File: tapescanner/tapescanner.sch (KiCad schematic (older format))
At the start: 49 parts, among them J0 USB_B, J2 AVR-ISP-10, M0 Motor_DC, Q0 TEPT5600, Q1 TEPT5600, Q10 MJE13007G, Q2 TEPT5600, Q3 TEPT5600, Q4 TEPT5600, Q5 TEPT5600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

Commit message: Fix RKM codes
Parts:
- C2: value 10nF -> 10n
- C3, C4: value 47pF -> 47p
- C5: value 4.7uF -> 4.7u
- C6: value 100nF -> 100n
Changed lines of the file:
@@
 P 3750 2500
 F 0 "C2" H 3865 2546 50  0000 L CNN
-F 1 "10nF" H 3865 2455 50  0000 L CNN
+F 1 "10n" H 3865 2455 50  0000 L CNN
 F 2 "" H 3788 2350 50  0001 C CNN
 F 3 "~" H 3750 2500 50  0001 C CNN
@@
 P 4200 2500
 F 0 "C3" H 4315 2546 50  0000 L CNN
-F 1 "47pF" H 4315 2455 50  0000 L CNN
+F 1 "47p" H 4315 2455 50  0000 L CNN
 F 2 "" H 4238 2350 50  0001 C CNN
 F 3 "~" H 4200 2500 50  0001 C CNN
@@
 P 4650 2500
 F 0 "C4" H 4765 2546 50  0000 L CNN
-F 1 "47pF" H 4765 2455 50  0000 L CNN
+F 1 "47p" H 4765 2455 50  0000 L CNN
 F 2 "" H 4688 2350 50  0001 C CNN
 F 3 "~" H 4650 2500 50  0001 C CNN
@@
 P 4900 1350
 F 0 "C6" H 5015 1396 50  0000 L CNN
-F 1 "100nF" H 5015 1305 50  0000 L CNN
+F 1 "100n" H 5015 1305 50  0000 L CNN
 F 2 "" H 4938 1200 50  0001 C CNN
 F 3 "~" H 4900 1350 50  0001 C CNN
@@
 U 1 1 6084B0AF
 P 4400 1350
-F 0 "C5" H 4518 1396 50  0000 L CNN
-F 1 "4.7uF" H 4518 1305 50  0000 L CNN
+F 0 "C5" H 4282 1304 50  0000 R CNN
+F 1 "4.7u" H 4282 1395 50  0000 R CNN
 F 2 "" H 4438 1200 50  0001 C CNN
 F 3 "~" H 4400 1350 50  0001 C CNN

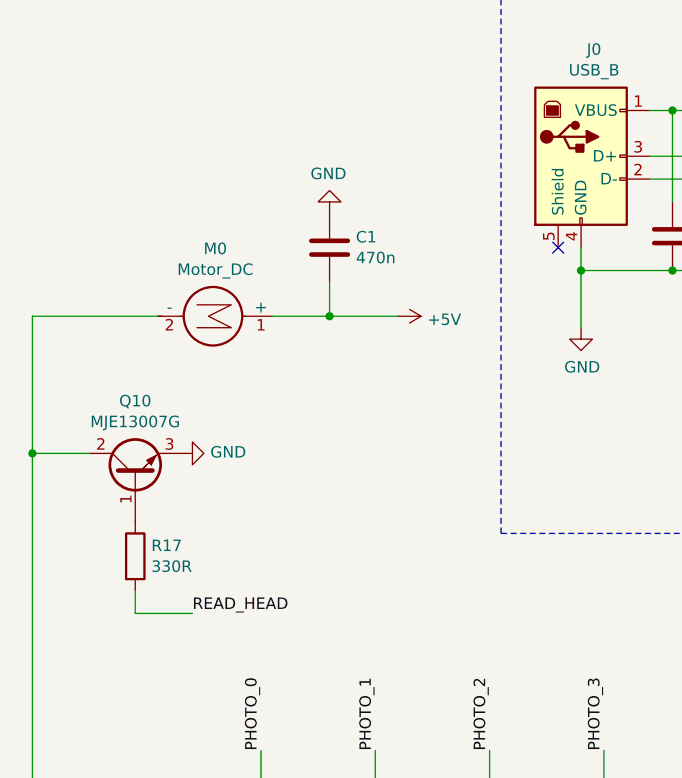
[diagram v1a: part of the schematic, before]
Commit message: Fix motor capacitor
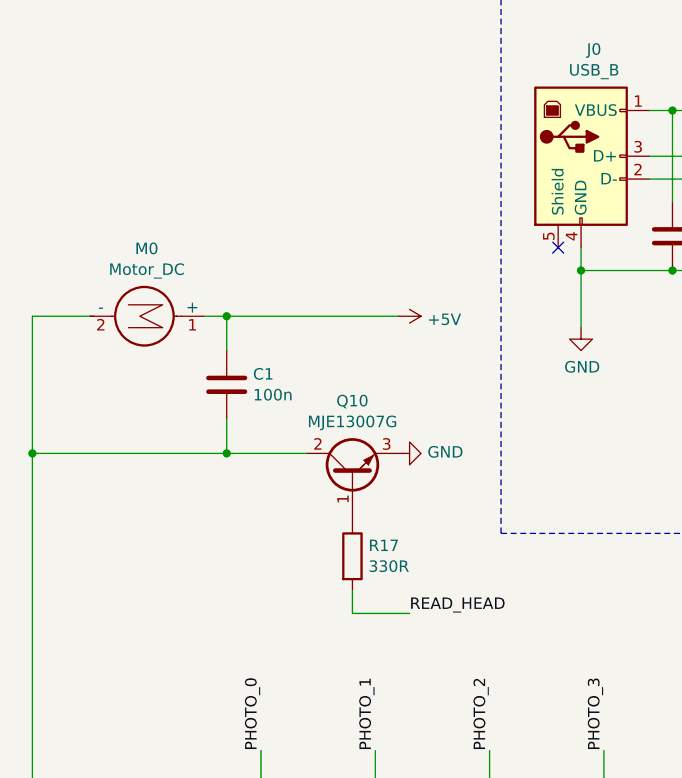
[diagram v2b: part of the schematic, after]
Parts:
- C1: value 470n -> 100n
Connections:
- net +5V: now also C1.1; no longer C1.2
- net GND: no longer C1.1
- net at D0.1 (K), D1.1 (K), D2.1 (K)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: now also C1.2
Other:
- moved on the sheet: M0, Q10, R17
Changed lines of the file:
@@
 L Transistor_BJT:MJE13007G Q10
 U 1 1 606AAE77
-P 1400 3550
-F 0 "Q10" V 1729 3550 50  0000 C CNN
-F 1 "MJE13007G" V 1638 3550 50  0000 C CNN
-F 2 "Package_TO_SOT_THT:TO-220-3_Vertical" H 1650 3475 50  0001 L CIN
-F 3 "http://www.onsemi.com/pub_link/Collateral/MJE13007-D.PDF" H 1400 3550 50  0001 L CNN
-	1    1400 3550
+P 2350 3550
+F 0 "Q10" V 2679 3550 50  0000 C CNN
+F 1 "MJE13007G" V 2588 3550 50  0000 C CNN
+F 2 "Package_TO_SOT_THT:TO-220-3_Vertical" H 2600 3475 50  0001 L CIN
+F 3 "http://www.onsemi.com/pub_link/Collateral/MJE13007-D.PDF" H 2350 3550 50  0001 L CNN
+	1    2350 3550
 	0    -1   -1   0
 $EndComp
@@
 L power:GND #PWR0101
 U 1 1 606B3702
-P 1600 3450
-F 0 "#PWR0101" H 1600 3200 50  0001 C CNN
-F 1 "GND" V 1605 3322 50  0000 R CNN
-F 2 "" H 1600 3450 50  0001 C CNN
-F 3 "" H 1600 3450 50  0001 C CNN
-	1    1600 3450
+P 2550 3450
+F 0 "#PWR0101" H 2550 3200 50  0001 C CNN
+F 1 "GND" V 2555 3322 50  0000 R CNN
+F 2 "" H 2550 3450 50  0001 C CNN
+F 3 "" H 2550 3450 50  0001 C CNN
+	1    2550 3450
 	0    -1   -1   0
 $EndComp
@@
 Connection ~ 1700 6200
 Wire Wire Line
-	1200 3450 950  3450
-Wire Wire Line
 	950  6650 1950 6650
 Wire Wire Line
@@
 L Device:R R17
 U 1 1 606CF734
-P 1400 3900
-F 0 "R17" H 1470 3946 50  0000 L CNN
-F 1 "330R" H 1470 3855 50  0000 L CNN
-F 2 "" V 1330 3900 50  0001 C CNN
-F 3 "~" H 1400 3900 50  0001 C CNN
-	1    1400 3900
-	1    0    0    -1
-$EndComp
-Wire Wire Line
-	1400 4050 1400 4150
-Wire Wire Line
-	1400 4150 1650 4150
-Text Label 1650 4150 0    50   ~ 0
+P 2350 3900
+F 0 "R17" H 2420 3946 50  0000 L CNN
+F 1 "330R" H 2420 3855 50  0000 L CNN
+F 2 "" V 2280 3900 50  0001 C CNN
+F 3 "~" H 2350 3900 50  0001 C CNN
+	1    2350 3900
+	1    0    0    -1
+$EndComp
+Wire Wire Line
+	2350 4050 2350 4150
+Wire Wire Line
+	2350 4150 2600 4150
+Text Label 2600 4150 0    50   ~ 0
 READ_HEAD
-Wire Wire Line
-	950  2850 1500 2850
-$Comp
-L Motor:Motor_DC M0
-U 1 1 606DC4B7
-P 1800 2850
-F 0 "M0" V 1505 2800 50  0000 C CNN
-F 1 "Motor_DC" V 1596 2800 50  0000 C CNN
-F 2 "" H 1800 2760 50  0001 C CNN
-F 3 "~" H 1800 2760 50  0001 C CNN
-	1    1800 2850
-	0    1    1    0
-$EndComp
-Wire Wire Line
-	2000 2850 2250 2850
-Wire Wire Line
-	2250 2850 2250 2700
-Connection ~ 2250 2850
-Wire Wire Line
-	2250 2850 2550 2850
-$Comp
-L Device:C C1
-U 1 1 606EDAE3
-P 2250 2550
-F 0 "C1" H 2365 2596 50  0000 L CNN
-F 1 "470n" H 2365 2505 50  0000 L CNN
-F 2 "" H 2288 2400 50  0001 C CNN
-F 3 "~" H 2250 2550 50  0001 C CNN
-	1    2250 2550
-	1    0    0    -1
-$EndComp
-$Comp
-L power:GND #PWR0104
-U 1 1 606EFFCB
-P 2250 2400
-F 0 "#PWR0104" H 2250 2150 50  0001 C CNN
-F 1 "GND" H 2255 2227 50  0000 C CNN
-F 2 "" H 2250 2400 50  0001 C CNN
-F 3 "" H 2250 2400 50  0001 C CNN
-	1    2250 2400
-	-1   0    0    1
-$EndComp
 $Comp
 L power:+5V #PWR0118
@@
 	0    1    1    0
 $EndComp
-Wire Wire Line
-	950  3450 950  6200
 Connection ~ 950  6200
-Wire Wire Line
-	950  2850 950  3450
-Connection ~ 950  3450
 $Comp
 L Device:C C2
@@
 Wire Wire Line
 	3350 2650 3350 2900
+Wire Wire Line
+	950  2850 950  3450
+Wire Wire Line
+	950  3450 1800 3450
+Connection ~ 950  3450
+Wire Wire Line
+	950  3450 950  6200
+$Comp
+L Motor:Motor_DC M0
+U 1 1 606DC4B7
+P 1500 2850
+F 0 "M0" V 1205 2800 50  0000 C CNN
+F 1 "Motor_DC" V 1296 2800 50  0000 C CNN
+F 2 "" H 1500 2760 50  0001 C CNN
+F 3 "~" H 1500 2760 50  0001 C CNN
+	1    1500 2850
+	0    1    1    0
+$EndComp
+Wire Wire Line
+	1200 2850 950  2850
+Wire Wire Line
+	1700 2850 1800 2850
+$Comp
+L Device:C C1
+U 1 1 6062ABC6
+P 1800 3150
+F 0 "C1" H 1915 3196 50  0000 L CNN
+F 1 "100n" H 1915 3105 50  0000 L CNN
+F 2 "" H 1838 3000 50  0001 C CNN
+F 3 "~" H 1800 3150 50  0001 C CNN
+	1    1800 3150
+	1    0    0    -1
+$EndComp
+Wire Wire Line
+	1800 3000 1800 2850
+Wire Wire Line
+	1800 3300 1800 3450
+Connection ~ 1800 2850
+Connection ~ 1800 3450
+Wire Wire Line
+	1800 2850 2550 2850
+Wire Wire Line
+	1800 3450 2150 3450
 $EndSCHEMATC

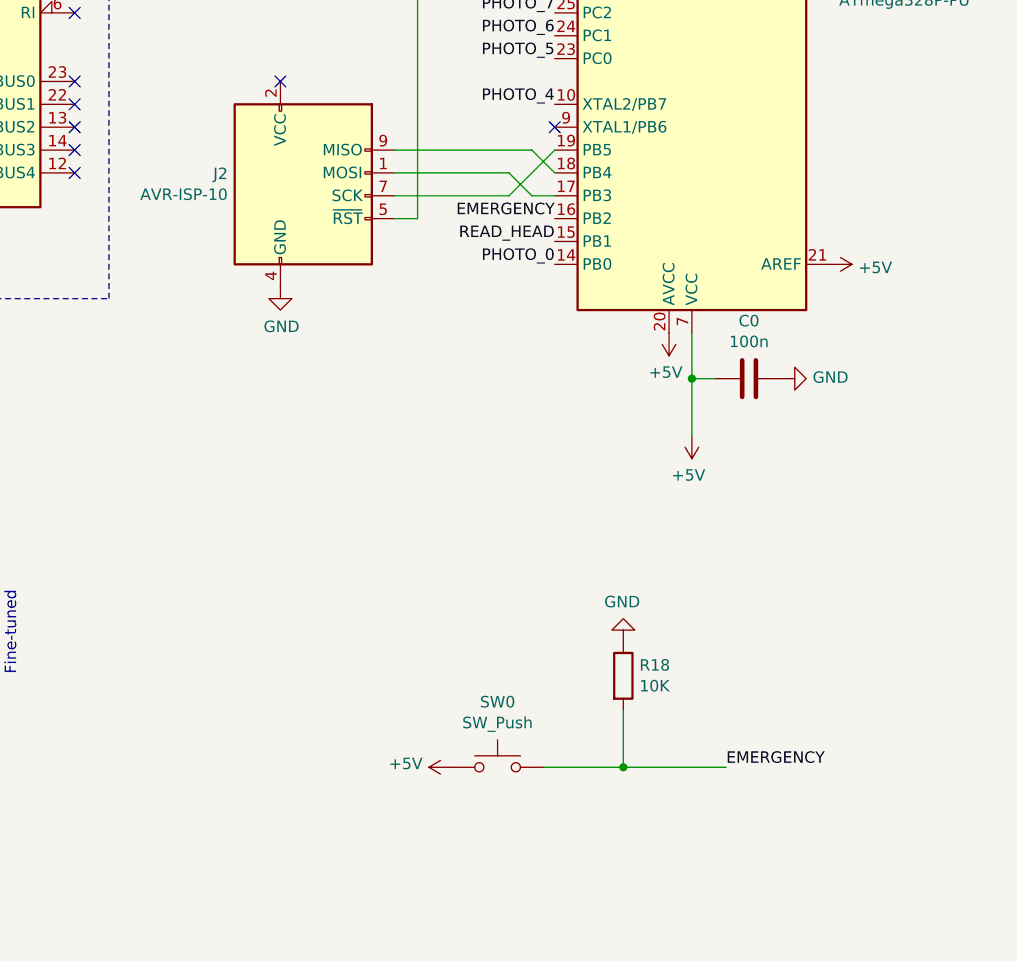
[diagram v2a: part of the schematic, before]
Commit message: Add power LED
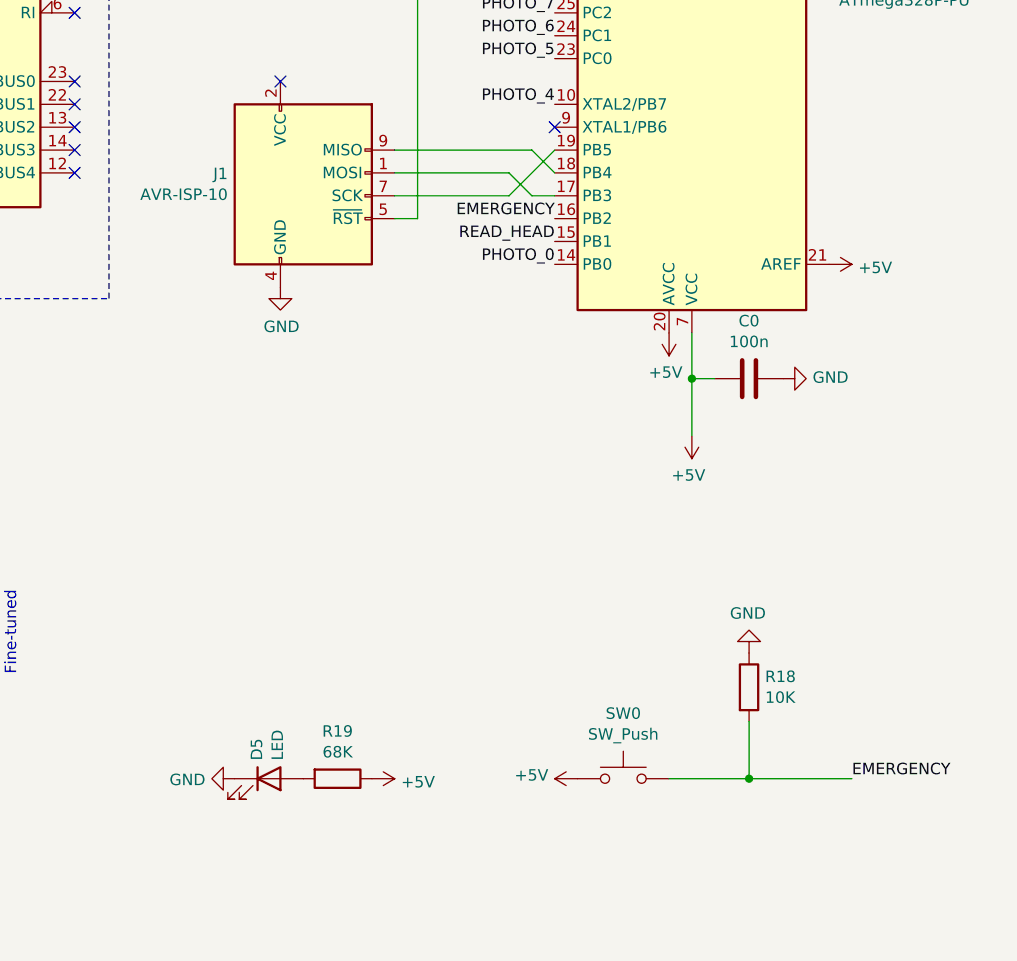
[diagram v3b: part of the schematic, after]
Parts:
- added D5: LED, symbol Device:LED
- added R19: 68K, symbol Device:R
- renumbered J2 to J1
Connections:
- net +5V: now also R19.1
- net GND: now also D5.1 (K)
- new net: D5.2 (A), R19.2
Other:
- moved on the sheet: R18, SW0
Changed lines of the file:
@@
 L Switch:SW_Push SW0
 U 1 1 60725EDE
-P 8850 5850
-F 0 "SW0" H 8850 6135 50  0000 C CNN
-F 1 "SW_Push" H 8850 6044 50  0000 C CNN
-F 2 "" H 8850 6050 50  0001 C CNN
-F 3 "~" H 8850 6050 50  0001 C CNN
-	1    8850 5850
+P 9400 5900
+F 0 "SW0" H 9400 6185 50  0000 C CNN
+F 1 "SW_Push" H 9400 6094 50  0000 C CNN
+F 2 "" H 9400 6100 50  0001 C CNN
+F 3 "~" H 9400 6100 50  0001 C CNN
+	1    9400 5900
 	1    0    0    -1
 $EndComp
@@
 L power:+5V #PWR0119
 U 1 1 60727D38
-P 8650 5850
-F 0 "#PWR0119" H 8650 5700 50  0001 C CNN
-F 1 "+5V" V 8665 5978 50  0000 L CNN
-F 2 "" H 8650 5850 50  0001 C CNN
-F 3 "" H 8650 5850 50  0001 C CNN
-	1    8650 5850
+P 9200 5900
+F 0 "#PWR0119" H 9200 5750 50  0001 C CNN
+F 1 "+5V" V 9215 6028 50  0000 L CNN
+F 2 "" H 9200 5900 50  0001 C CNN
+F 3 "" H 9200 5900 50  0001 C CNN
+	1    9200 5900
 	0    -1   -1   0
 $EndComp
-Text Label 9850 5850 0    50   ~ 0
+Text Label 10400 5900 0    50   ~ 0
 EMERGENCY
 $Comp
 L Device:R R18
 U 1 1 60739369
-P 9400 5450
-F 0 "R18" H 9470 5496 50  0000 L CNN
-F 1 "10K" H 9470 5405 50  0000 L CNN
-F 2 "" V 9330 5450 50  0001 C CNN
-F 3 "~" H 9400 5450 50  0001 C CNN
-	1    9400 5450
+P 9950 5500
+F 0 "R18" H 10020 5546 50  0000 L CNN
+F 1 "10K" H 10020 5455 50  0000 L CNN
+F 2 "" V 9880 5500 50  0001 C CNN
+F 3 "~" H 9950 5500 50  0001 C CNN
+	1    9950 5500
 	1    0    0    -1
 $EndComp
@@
 L power:GND #PWR0120
 U 1 1 6073B5AB
-P 9400 5300
-F 0 "#PWR0120" H 9400 5050 50  0001 C CNN
-F 1 "GND" H 9405 5127 50  0000 C CNN
-F 2 "" H 9400 5300 50  0001 C CNN
-F 3 "" H 9400 5300 50  0001 C CNN
-	1    9400 5300
+P 9950 5350
+F 0 "#PWR0120" H 9950 5100 50  0001 C CNN
+F 1 "GND" H 9955 5177 50  0000 C CNN
+F 2 "" H 9950 5350 50  0001 C CNN
+F 3 "" H 9950 5350 50  0001 C CNN
+	1    9950 5350
 	-1   0    0    1
 $EndComp
 Wire Wire Line
-	9050 5850 9400 5850
+	9600 5900 9950 5900
 Wire Wire Line
-	9400 5600 9400 5850
-Connection ~ 9400 5850
+	9950 5650 9950 5900
+Connection ~ 9950 5900
 Wire Wire Line
-	9400 5850 9850 5850
+	9950 5900 10400 5900
 $Comp
-L Connector:AVR-ISP-10 J2
+L Connector:AVR-ISP-10 J1
 U 1 1 6081F6F5
 P 8000 3350
-F 0 "J2" H 7670 3446 50  0000 R CNN
+F 0 "J1" H 7670 3446 50  0000 R CNN
 F 1 "AVR-ISP-10" H 7670 3355 50  0000 R CNN
 F 2 "" V 7750 3400 50  0001 C CNN
@@
 Wire Wire Line
 	1800 3450 2150 3450
+$Comp
+L Device:LED D5
+U 1 1 60649787
+P 7850 5900
+F 0 "D5" V 7797 5980 50  0000 L CNN
+F 1 "LED" V 7888 5980 50  0000 L CNN
+F 2 "" H 7850 5900 50  0001 C CNN
+F 3 "~" H 7850 5900 50  0001 C CNN
+	1    7850 5900
+	1    0    0    -1
+$EndComp
+$Comp
+L power:GND #PWR0104
+U 1 1 606583DC
+P 7700 5900
+F 0 "#PWR0104" H 7700 5650 50  0001 C CNN
+F 1 "GND" V 7705 5772 50  0000 R CNN
+F 2 "" H 7700 5900 50  0001 C CNN
+F 3 "" H 7700 5900 50  0001 C CNN
+	1    7700 5900
+	0    1    1    0
+$EndComp
+$Comp
+L Device:R R19
+U 1 1 6066003C
+P 8150 5900
+F 0 "R19" V 7943 5900 50  0000 C CNN
+F 1 "68K" V 8034 5900 50  0000 C CNN
+F 2 "" V 8080 5900 50  0001 C CNN
+F 3 "~" H 8150 5900 50  0001 C CNN
+	1    8150 5900
+	0    1    1    0
+$EndComp
+$Comp
+L power:+5V #PWR0123
+U 1 1 60660F2E
+P 8300 5900
+F 0 "#PWR0123" H 8300 5750 50  0001 C CNN
+F 1 "+5V" V 8315 6028 50  0000 L CNN
+F 2 "" H 8300 5900 50  0001 C CNN
+F 3 "" H 8300 5900 50  0001 C CNN
+	1    8300 5900
+	0    1    1    0
+$EndComp
 $EndSCHEMATC

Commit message: Readjust resistors
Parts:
- R11: value 120K -> 180K
- R7: value 47K -> 68K
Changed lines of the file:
@@
 P 2200 5200
 F 0 "R7" H 2270 5246 50  0000 L CNN
-F 1 "47K" H 2270 5155 50  0000 L CNN
+F 1 "68K" H 2270 5155 50  0000 L CNN
 F 2 "" V 2130 5200 50  0001 C CNN
 F 3 "~" H 2200 5200 50  0001 C CNN
@@
 P 4200 5200
 F 0 "R11" H 4270 5246 50  0000 L CNN
-F 1 "120K" H 4270 5155 50  0000 L CNN
+F 1 "180K" H 4270 5155 50  0000 L CNN
 F 2 "" V 4130 5200 50  0001 C CNN
 F 3 "~" H 4200 5200 50  0001 C CNN

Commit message: Adjust connections
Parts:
- R7: value 68K -> 82K
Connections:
- net +5V: no longer U0.21 (AREF)
- no-connect marks 21 -> 23
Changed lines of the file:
@@
-$EndComp
-$Comp
-L power:+5V #PWR0108
-U 1 1 607CA28C
-P 10300 3650
-F 0 "#PWR0108" H 10300 3500 50  0001 C CNN
-F 1 "+5V" V 10315 3778 50  0000 L CNN
-F 2 "" H 10300 3650 50  0001 C CNN
-F 3 "" H 10300 3650 50  0001 C CNN
-	1    10300 3650
-	0    1    1    0
 $EndComp
 $Comp
@@
 P 2200 5200
 F 0 "R7" H 2270 5246 50  0000 L CNN
-F 1 "68K" H 2270 5155 50  0000 L CNN
+F 1 "82K" H 2270 5155 50  0000 L CNN
 F 2 "" V 2130 5200 50  0001 C CNN
 F 3 "~" H 2200 5200 50  0001 C CNN
@@
 	0    1    1    0
 $EndComp
+NoConn ~ 10300 3650
+NoConn ~ -1300 5300
 $EndSCHEMATC
